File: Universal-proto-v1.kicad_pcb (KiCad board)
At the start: 2 copper layers, 81.5 x 121 mm, 44 parts, among them J1 Bus_ISA_8bit, J2 ISA Breakout, J3 Pico GPIO Breakout

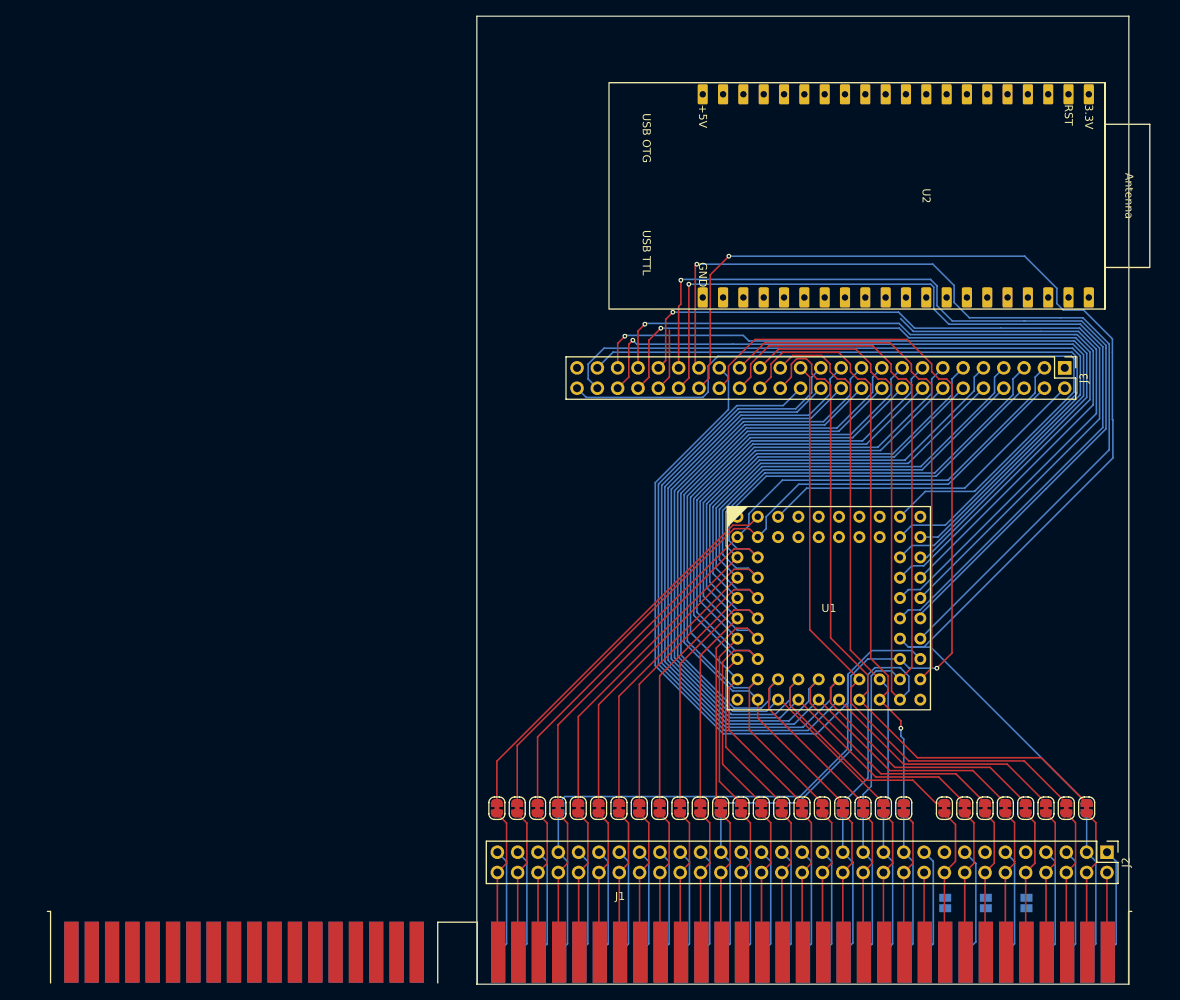
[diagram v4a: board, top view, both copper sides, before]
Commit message: Connect some grounds
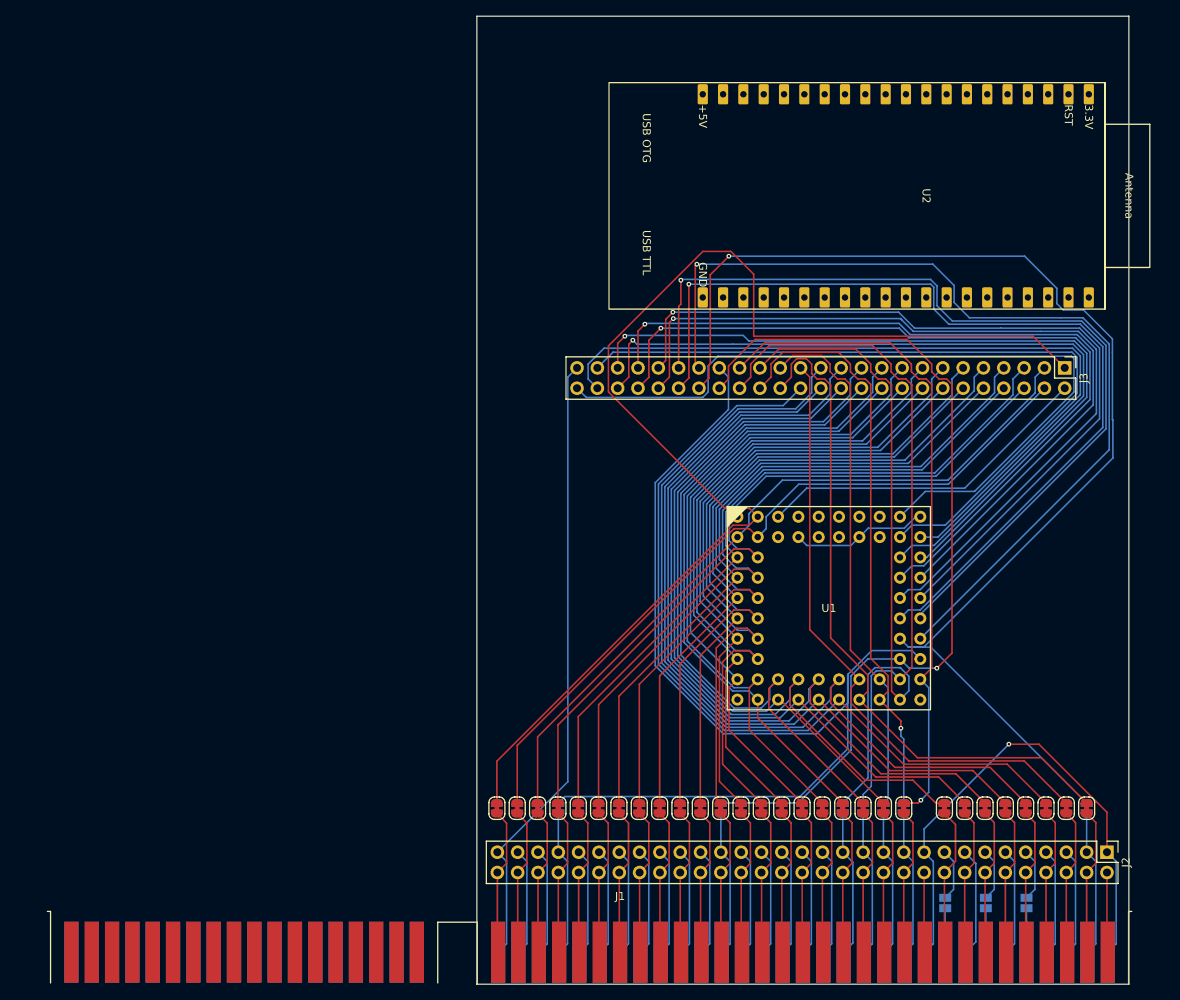
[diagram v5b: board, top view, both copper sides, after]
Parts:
- turned JP37 to -90 degrees
- turned JP38 to -90 degrees
- turned JP39 to -90 degrees
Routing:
- net /GND: track 40.2 -> 160.7 mm, vias 0 -> 1
- net /GP0_ISA_A0: track 50.5 -> 153.9 mm
- net /GP39: track 76.0 -> 106.3 mm, vias 0 -> 1
- net /GP32_ISA_AEN: track 65.5 -> 83.7 mm, vias 0 -> 1
- net /HDR_-5V: track 0.00 -> 6.61 mm
- net /HDR_+12V: track 0.00 -> 6.61 mm
- net /HDR_-12V: track 0.00 -> 6.61 mm
- net /ISA_-5V: track 0.00 -> 5.50 mm
- net /ISA_-12V: track 0.00 -> 5.50 mm
- net /ISA_+12V: track 0.00 -> 5.50 mm

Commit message: Most everything connected.
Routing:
- net /GND: track 160.7 -> 260.6 mm, vias 1 -> 3
- net /GP0_ISA_A0: track 153.9 -> 97.5 mm
- net /GP21_ISA_D1: track 93.7 -> 96.8 mm
- net /GP16_ISA_A16: track 84.1 -> 87.0 mm
- net /GP15_ISA_A15: track 77.0 -> 79.8 mm
- net /GP1_ISA_A1: track 93.3 -> 95.7 mm
- net /GP12_ISA_A12: track 80.0 -> 82.0 mm
- net /GP8_ISA_A8: track 84.3 -> 86.3 mm
- net /GP18_ISA_A18: track 91.0 -> 92.9 mm
- net /GP20_ISA_D0: track 100.9 -> 102.8 mm
- net /GP11_ISA_A11: track 82.9 -> 84.7 mm
- net /GP22_ISA_D2: track 105.9 -> 107.7 mm
- net /GP13_ISA_A13: track 83.1 -> 84.9 mm
- net /GP19_ISA_A19: track 83.4 -> 85.1 mm
- net /GP14_ISA_A14: track 80.1 -> 81.7 mm
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
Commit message: Everything connected.
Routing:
- net /VCC: track 27.0 -> 95.4 mm
- net /GND: track 260.6 -> 261.8 mm, vias 3 -> 5
- net /ALE: track 18.3 -> 18.5 mm, vias 0 -> 2
- net /~{SMEMR}: track 18.3 -> 18.5 mm, vias 0 -> 2
- net /~{IOW}: track 18.3 -> 18.5 mm, vias 0 -> 2
- net /~{IOR}: track 18.4 -> 18.6 mm, vias 0 -> 2
- net /~{SMEMW}: track 18.3 -> 18.4 mm, vias 0 -> 2
- net /CLK: vias 0 -> 2

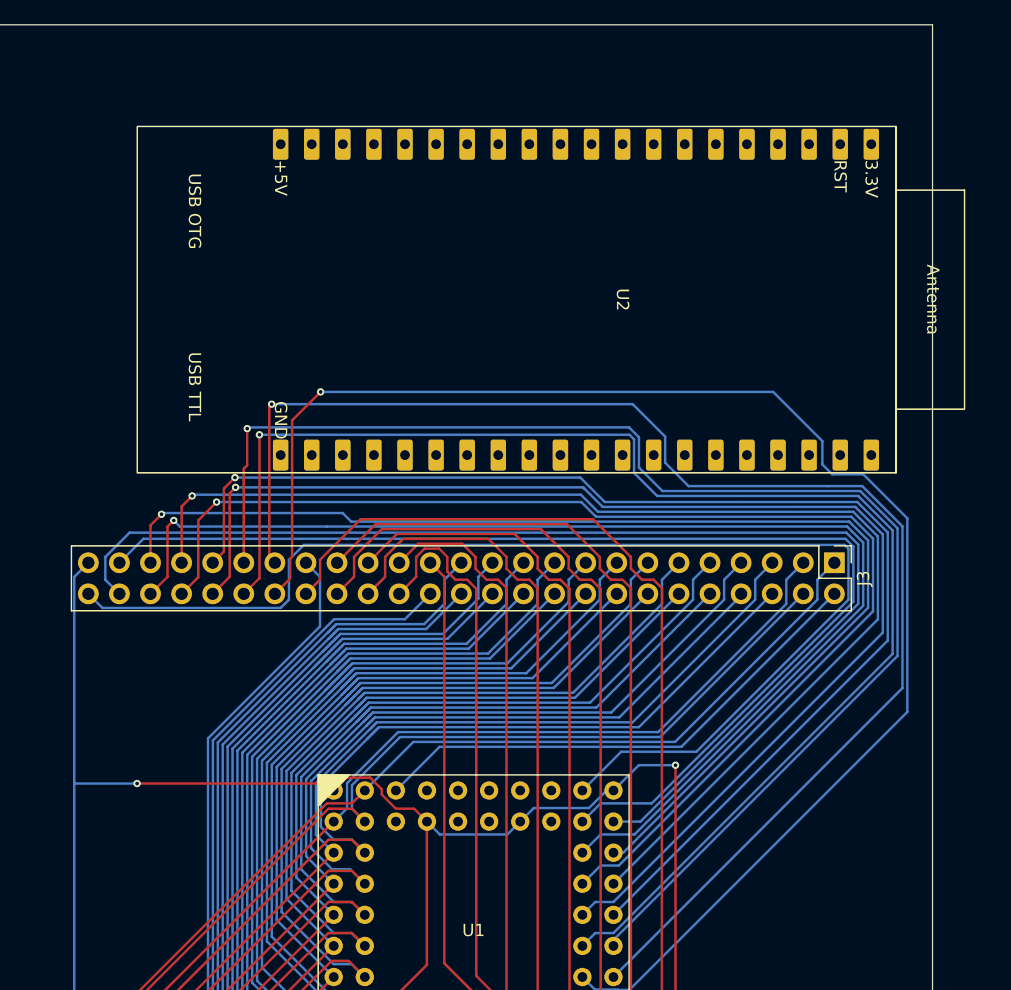
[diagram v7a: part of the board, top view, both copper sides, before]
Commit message: Added GPIO labels
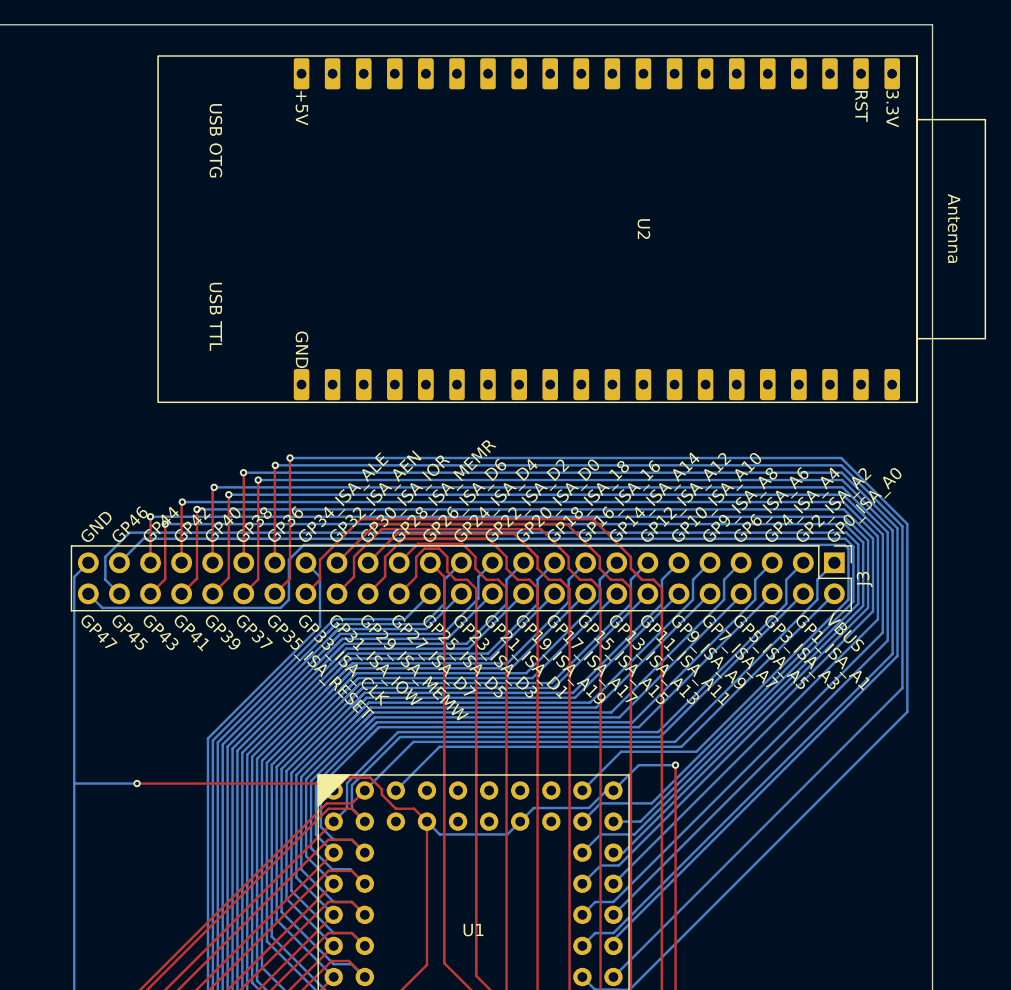
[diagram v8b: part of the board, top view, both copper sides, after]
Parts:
- moved U2 6.01 mm to (185.2, 27.0)
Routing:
- net /GP36: track 116.8 -> 108.5 mm
- net /GP35_ISA_RESET: track 153.1 -> 145.5 mm
- net /GP37: track 115.4 -> 108.7 mm
- net /GP38: track 112.9 -> 106.4 mm
- net /GP39: track 106.3 -> 105.6 mm
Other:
- board text added: "GND"
- board text added: "GP0_ISA_A0"
- board text added: "GP10_ISA_A10"
- board text added: "GP11_ISA_A11"
- board text added: "GP12_ISA_A12"
- board text added: "GP13_ISA_A13"
- board text added: "GP14_ISA_A14"
- board text added: "GP15_ISA_A15"
- board text added: "GP16_ISA_16"
- board text added: "GP17_ISA_A17"
- board text added: "GP18_ISA_18"
- board text added: "GP19_ISA_A19"
- board text added: "GP1_ISA_A1"
- board text added: "GP20_ISA_D0"
- board text added: "GP21_ISA_D1"
- board text added: "GP22_ISA_D2"
- board text added: "GP23_ISA_D3"
- board text added: "GP24_ISA_D4"
- board text added: "GP25_ISA_D5"
- board text added: "GP26_ISA_D6"
- board text added: "GP27_ISA_D7"
- board text added: "GP28_ISA_MEMR"
- board text added: "GP29_ISA_MEMW"
- board text added: "GP2_ISA_A2"
- board text added: "GP30_ISA_IOR"
- board text added: "GP31_ISA_IOW"
- board text added: "GP32_ISA_AEN"
- board text added: "GP33_ISA_CLK"
- board text added: "GP34_ISA_ALE"
- board text added: "GP35_ISA_RESET"
- board text added: "GP36"
- board text added: "GP37"
- board text added: "GP38"
- board text added: "GP39"
- board text added: "GP3_ISA_A3"
- board text added: "GP40"
- board text added: "GP41"
- board text added: "GP42"
- board text added: "GP43"
- board text added: "GP44"
- board text added: "GP45"
- board text added: "GP46"
- board text added: "GP47"
- board text added: "GP4_ISA_A4"
- board text added: "GP5_ISA_A5"
- board text added: "GP6_ISA_A6"
- board text added: "GP7_ISA_A7"
- board text added: "GP9_ISA_A8"
- board text added: "GP9_ISA_A9"
- board text added: "VBUS"
